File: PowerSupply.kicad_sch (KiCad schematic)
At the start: 31 parts, among them J1 B2B-PH-K-S, J2 Native USB, J3 Native USB, SW1 SSSS213000, U1 CH340E, U2 NCP1117-5.0_SOT223, U3 TPS2115ADRBR, U4 ld39150dt33-r, U5 USBLC6-2SC6, U6 USBLC6-2SC6

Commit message: update for production
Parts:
- renumbered Serial to Serial1
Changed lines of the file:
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@@
 		(on_board yes)
 		(dnp no)
-		(property "Reference" "#PWR0103"
+		(property "Reference" "#PWR024"
 			(at 107.95 179.07 0)
 			(effects
@@
 			(project "MX_IMU"
 				(path "/8ed38441-7d4e-4e89-870f-07e11c6dce38/623e427f-6907-46a8-ba12-bccc1b1d2c2b"
-					(reference "#PWR0103")
+					(reference "#PWR024")
 					(unit 1)
 				)
@@
 		(dnp no)
 		(fields_autoplaced yes)
-		(property "Reference" "#PWR030"
+		(property "Reference" "#PWR033"
 			(at 209.55 52.07 0)
 			(effects
@@
 			(project "MX_IMU"
 				(path "/8ed38441-7d4e-4e89-870f-07e11c6dce38/623e427f-6907-46a8-ba12-bccc1b1d2c2b"
-					(reference "#PWR030")
+					(reference "#PWR033")
 					(unit 1)
 				)
@@
 		(on_board yes)
 		(dnp no)
-		(property "Reference" "#PWR029"
+		(property "Reference" "#PWR032"
 			(at 166.37 143.51 0)
 			(effects
@@
 			(project "MX_IMU"
 				(path "/8ed38441-7d4e-4e89-870f-07e11c6dce38/623e427f-6907-46a8-ba12-bccc1b1d2c2b"
-					(reference "#PWR029")
+					(reference "#PWR032")
 					(unit 1)
 				)
@@
 		(dnp no)
 		(fields_autoplaced yes)
-		(property "Reference" "#PWR031"
+		(property "Reference" "#PWR034"
 			(at 209.55 114.3 0)
 			(effects
@@
 			(project "MX_IMU"
 				(path "/8ed38441-7d4e-4e89-870f-07e11c6dce38/623e427f-6907-46a8-ba12-bccc1b1d2c2b"
-					(reference "#PWR031")
+					(reference "#PWR034")
 					(unit 1)
 				)
@@
 		(dnp no)
 		(fields_autoplaced yes)
-		(property "Reference" "#PWR027"
+		(property "Reference" "#PWR030"
 			(at 138.43 111.76 0)
 			(effects
@@
 			(project "MX_IMU"
 				(path "/8ed38441-7d4e-4e89-870f-07e11c6dce38/623e427f-6907-46a8-ba12-bccc1b1d2c2b"
-					(reference "#PWR027")
+					(reference "#PWR030")
 					(unit 1)
 				)
@@
 		(on_board yes)
 		(dnp no)
-		(property "Reference" "#PWR024"
+		(property "Reference" "#PWR027"
 			(at 128.27 50.8 0)
 			(effects
@@
 			(project "MX_IMU"
 				(path "/8ed38441-7d4e-4e89-870f-07e11c6dce38/623e427f-6907-46a8-ba12-bccc1b1d2c2b"
-					(reference "#PWR024")
+					(reference "#PWR027")
 					(unit 1)
 				)
@@
 		(dnp no)
 		(fields_autoplaced yes)
-		(property "Reference" "#PWR032"
+		(property "Reference" "#PWR035"
 			(at 214.63 52.07 0)
 			(effects
@@
 			(project "MX_IMU"
 				(path "/8ed38441-7d4e-4e89-870f-07e11c6dce38/623e427f-6907-46a8-ba12-bccc1b1d2c2b"
-					(reference "#PWR032")
+					(reference "#PWR035")
 					(unit 1)
 				)
@@
 		(dnp no)
 		(fields_autoplaced yes)
-		(property "Reference" "#PWR034"
+		(property "Reference" "#PWR037"
 			(at 231.14 77.47 0)
 			(effects
@@
 			(project "MX_IMU"
 				(path "/8ed38441-7d4e-4e89-870f-07e11c6dce38/623e427f-6907-46a8-ba12-bccc1b1d2c2b"
-					(reference "#PWR034")
+					(reference "#PWR037")
 					(unit 1)
 				)
@@
 		(on_board yes)
 		(dnp no)
-		(property "Reference" "#PWR022"
+		(property "Reference" "#PWR025"
 			(at 102.87 50.8 0)
 			(effects
@@
 			(project "MX_IMU"
 				(path "/8ed38441-7d4e-4e89-870f-07e11c6dce38/623e427f-6907-46a8-ba12-bccc1b1d2c2b"
-					(reference "#PWR022")
+					(reference "#PWR025")
 					(unit 1)
 				)
@@
 		(dnp no)
 		(fields_autoplaced yes)
-		(property "Reference" "#PWR036"
+		(property "Reference" "#PWR039"
 			(at 251.46 130.81 0)
 			(effects
@@
 			(project "MX_IMU"
 				(path "/8ed38441-7d4e-4e89-870f-07e11c6dce38/623e427f-6907-46a8-ba12-bccc1b1d2c2b"
-					(reference "#PWR036")
+					(reference "#PWR039")
 					(unit 1)
 				)
@@
 		(on_board yes)
 		(dnp no)
-		(property "Reference" "Serial"
+		(property "Reference" "Serial1"
 			(at 89.154 171.45 0)
 			(effects
@@
 			(project "MX_IMU"
 				(path "/8ed38441-7d4e-4e89-870f-07e11c6dce38/623e427f-6907-46a8-ba12-bccc1b1d2c2b"
-					(reference "Serial")
+					(reference "Serial1")
 					(unit 1)
 				)
@@
 		(dnp no)
 		(fields_autoplaced yes)
-		(property "Reference" "#PWR023"
+		(property "Reference" "#PWR026"
 			(at 115.57 76.2 0)
 			(effects
@@
 			(project "MX_IMU"
 				(path "/8ed38441-7d4e-4e89-870f-07e11c6dce38/623e427f-6907-46a8-ba12-bccc1b1d2c2b"
-					(reference "#PWR023")
+					(reference "#PWR026")
 					(unit 1)
 				)
@@
 		(dnp no)
 		(fields_autoplaced yes)
-		(property "Reference" "#PWR033"
+		(property "Reference" "#PWR036"
 			(at 214.63 114.3 0)
 			(effects
@@
 			(project "MX_IMU"
 				(path "/8ed38441-7d4e-4e89-870f-07e11c6dce38/623e427f-6907-46a8-ba12-bccc1b1d2c2b"
-					(reference "#PWR033")
+					(reference "#PWR036")
 					(unit 1)
 				)
@@
 		(on_board yes)
 		(dnp no)
-		(property "Reference" "#PWR0102"
+		(property "Reference" "#PWR022"
 			(at 83.82 190.5 0)
 			(effects
@@
 			(project "MX_IMU"
 				(path "/8ed38441-7d4e-4e89-870f-07e11c6dce38/623e427f-6907-46a8-ba12-bccc1b1d2c2b"
-					(reference "#PWR0102")
+					(reference "#PWR022")
 					(unit 1)
 				)
@@
 		(on_board yes)
 		(dnp no)
-		(property "Reference" "#PWR0101"
+		(property "Reference" "#PWR021"
 			(at 83.82 180.34 0)
 			(effects
@@
 			(project "MX_IMU"
 				(path "/8ed38441-7d4e-4e89-870f-07e11c6dce38/623e427f-6907-46a8-ba12-bccc1b1d2c2b"
-					(reference "#PWR0101")
+					(reference "#PWR021")
 					(unit 1)
 				)
@@
 		(dnp no)
 		(fields_autoplaced yes)
-		(property "Reference" "#PWR025"
+		(property "Reference" "#PWR028"
 			(at 130.81 111.76 0)
 			(effects
@@
 			(project "MX_IMU"
 				(path "/8ed38441-7d4e-4e89-870f-07e11c6dce38/623e427f-6907-46a8-ba12-bccc1b1d2c2b"
-					(reference "#PWR025")
+					(reference "#PWR028")
 					(unit 1)
 				)
@@
 		(dnp no)
 		(fields_autoplaced yes)
-		(property "Reference" "#PWR035"
+		(property "Reference" "#PWR038"
 			(at 251.46 66.04 0)
 			(effects
@@
 			(project "MX_IMU"
 				(path "/8ed38441-7d4e-4e89-870f-07e11c6dce38/623e427f-6907-46a8-ba12-bccc1b1d2c2b"
-					(reference "#PWR035")
+					(reference "#PWR038")
 					(unit 1)
 				)
@@
 		(dnp no)
 		(fields_autoplaced yes)
-		(property "Reference" "#PWR026"
+		(property "Reference" "#PWR029"
 			(at 138.43 91.44 0)
 			(effects
@@
 			(project "MX_IMU"
 				(path "/8ed38441-7d4e-4e89-870f-07e11c6dce38/623e427f-6907-46a8-ba12-bccc1b1d2c2b"
-					(reference "#PWR026")
+					(reference "#PWR029")
 					(unit 1)
 				)
@@
 		(on_board yes)
 		(dnp no)
-		(property "Reference" "#PWR028"
+		(property "Reference" "#PWR031"
 			(at 166.37 81.28 0)
 			(effects
@@
 			(project "MX_IMU"
 				(path "/8ed38441-7d4e-4e89-870f-07e11c6dce38/623e427f-6907-46a8-ba12-bccc1b1d2c2b"
-					(reference "#PWR028")
+					(reference "#PWR031")
 					(unit 1)
 				)
@@
 		(dnp no)
 		(fields_autoplaced yes)
-		(property "Reference" "#PWR021"
+		(property "Reference" "#PWR023"
 			(at 86.36 121.92 0)
 			(effects
@@
 			(project "MX_IMU"
 				(path "/8ed38441-7d4e-4e89-870f-07e11c6dce38/623e427f-6907-46a8-ba12-bccc1b1d2c2b"
-					(reference "#PWR021")
+					(reference "#PWR023")
 					(unit 1)
 				)

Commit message: PumbaaV2_RC2
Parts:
- C7: JLCPCB part (none) -> C15849
- R2, R3: value 330 -> 330R
- Serial1: value SM04B-GHS-TB -> SM04B-GHS-TB(LF)(SN)
- U2: value NCP1117-5.0_SOT223 -> NCP1117ST50T3G; JLCPCB Part (none) -> C17314
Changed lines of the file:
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@@
 			)
 		)
-		(property "Value" "NCP1117-5.0_SOT223"
+		(property "Value" "NCP1117ST50T3G"
 			(at 69.85 51.5421 0)
 			(effects
@@
 					(size 1.27 1.27)
 				)
+			)
+		)
+		(property "JLCPCB Part" "C17314"
+			(at 69.85 54.61 0)
+			(effects
+				(font
+					(size 1.27 1.27)
+				)
+				(hide yes)
 			)
 		)
@@
 			)
 		)
+		(property "JLCPCB part" "C15849"
+			(at 102.87 59.69 0)
+			(effects
+				(font
+					(size 1.27 1.27)
+				)
+				(hide yes)
+			)
+		)
 		(pin "1"
 		)
@@
 			)
 		)
-		(property "Value" "330"
+		(property "Value" "330R"
 			(at 71.12 149.86 0)
 			(effects
@@
 			)
 		)
-		(property "Value" "330"
+		(property "Value" "330R"
 			(at 62.23 149.86 0)
 			(effects
@@
 			)
 		)
-		(property "Value" "SM04B-GHS-TB"
+		(property "Value" "SM04B-GHS-TB(LF)(SN)"
 			(at 97.79 181.6099 0)
 			(effects

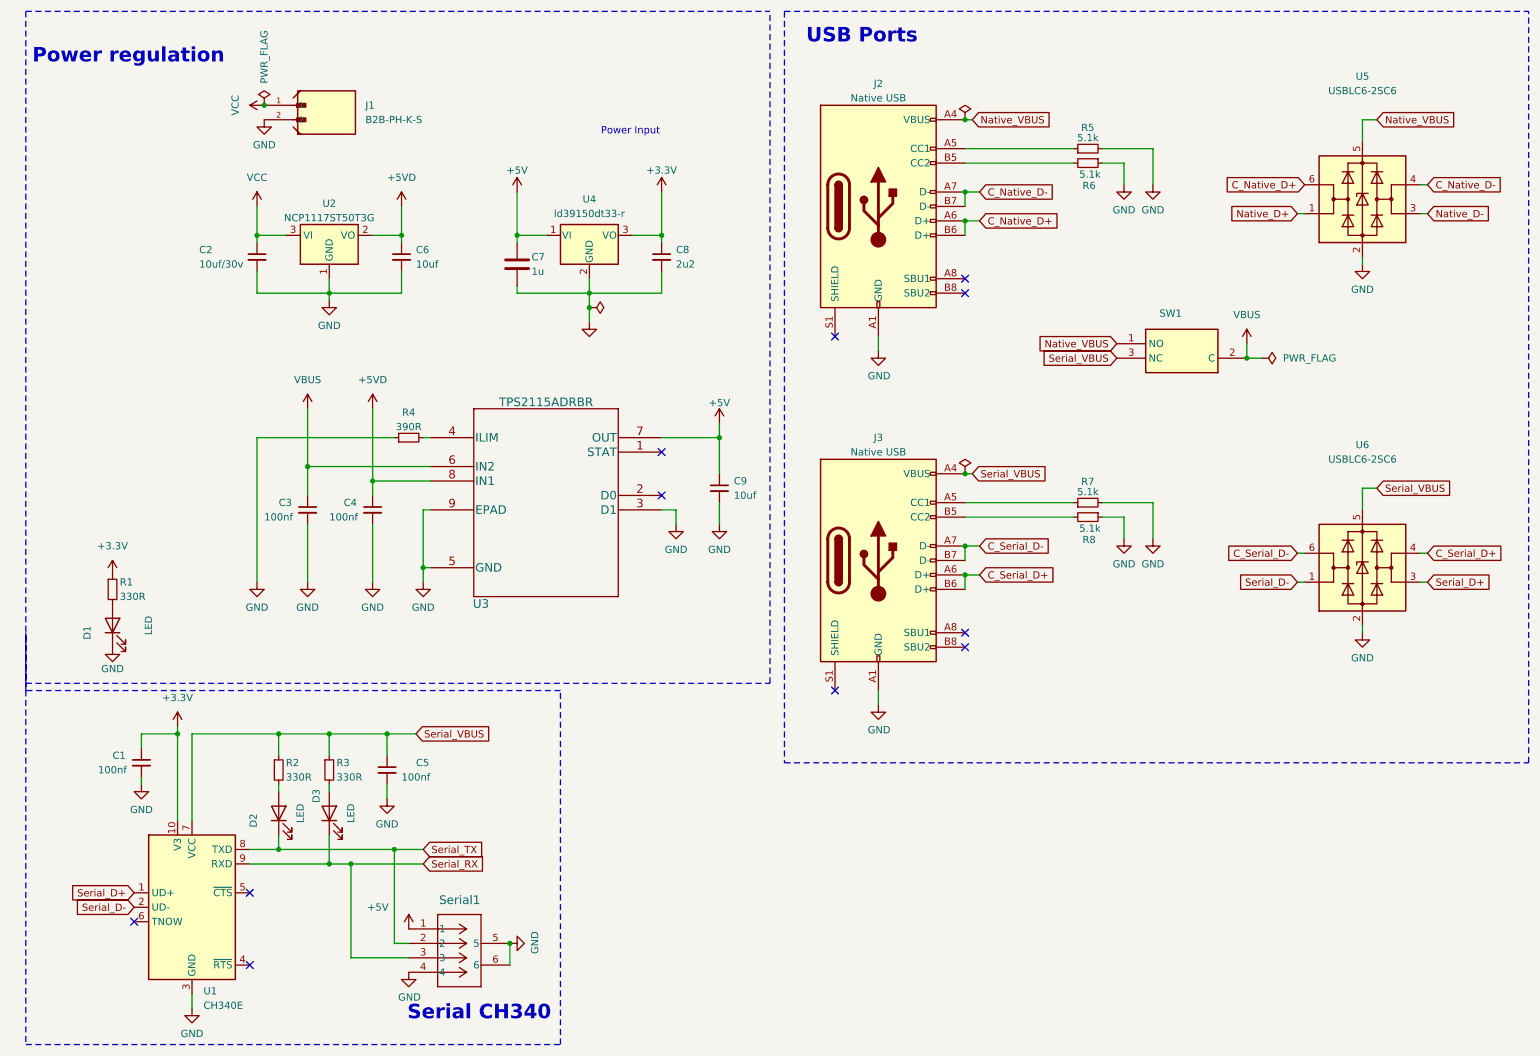
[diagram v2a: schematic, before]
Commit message: compact  IMU module for integration
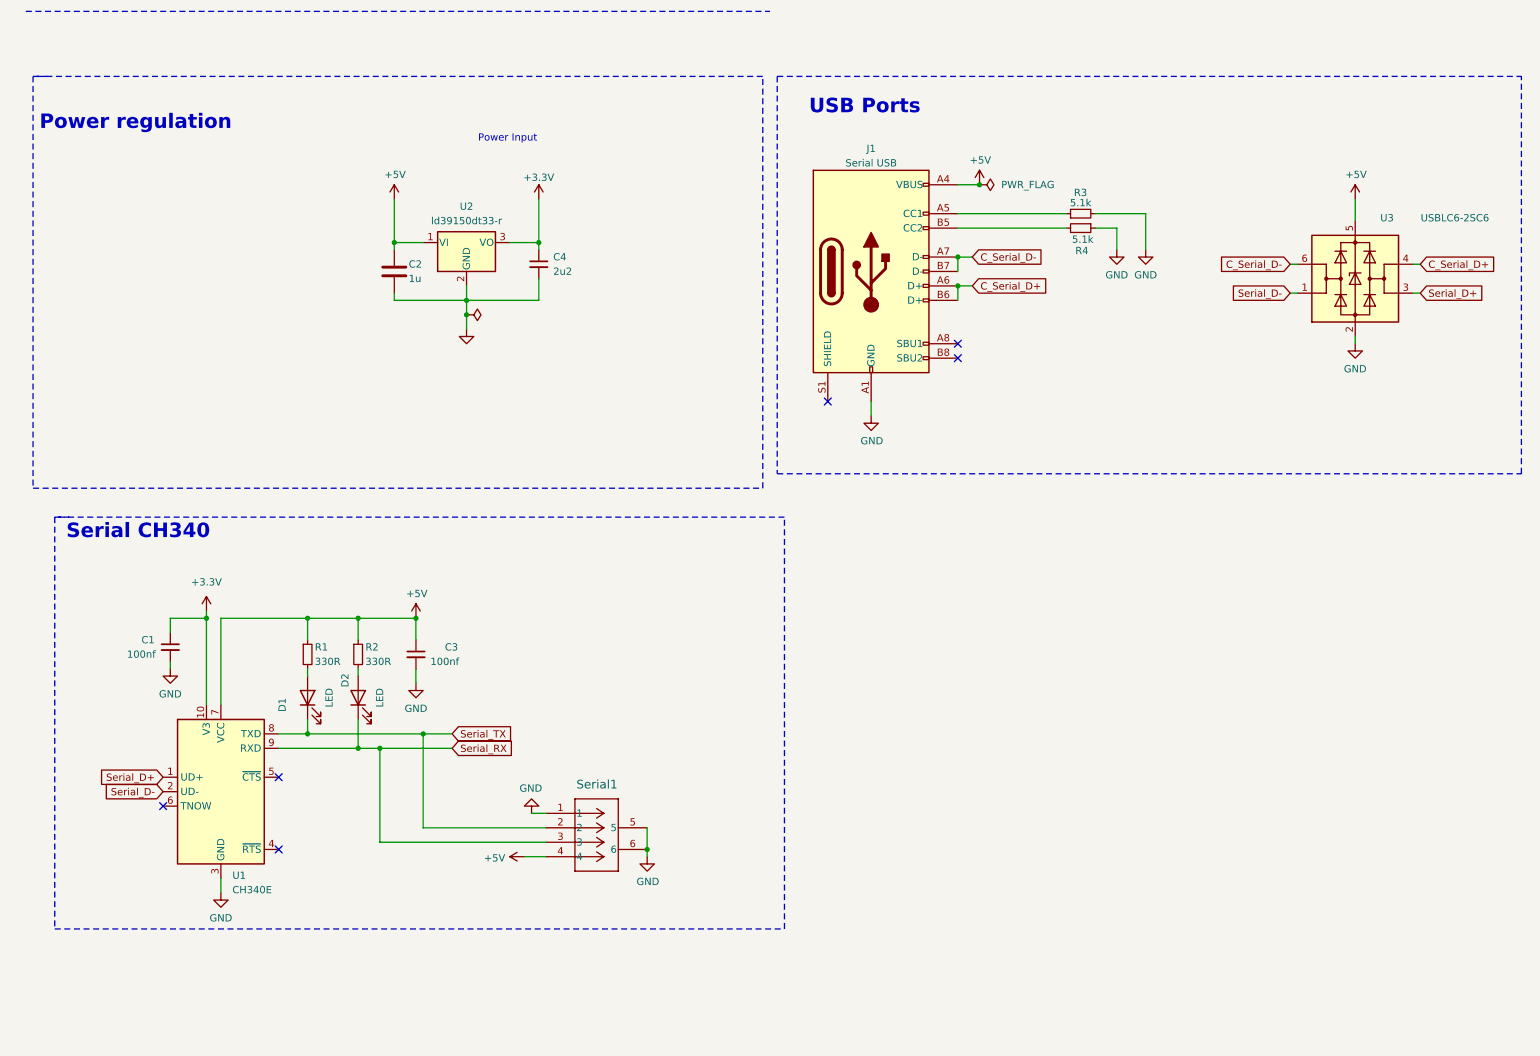
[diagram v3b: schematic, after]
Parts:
- removed C2: 10uf/30v, Capacitor_SMD:C_0805_2012Metric, symbol Device:C_Small
- removed C3, C4: 100nf, Capacitor_SMD:C_0603_1608Metric, symbol Device:C_Small
- removed C6, C9: 10uf, Capacitor_SMD:C_0603_1608Metric, symbol Device:C_Small
- removed D1: LED, LED_SMD:LED_0603_1608Metric, symbol Device:LED
- removed J1: B2B-PH-K-S, mylib:JST_B2B-PH-K-S, symbol B2B-PH-K-S:B2B-PH-K-S
- removed J2: Native USB, Connector_USB:USB_C_Receptacle_HRO_TYPE-C-31-M-12, symbol usb_c_receptacle_usb2.0:USB_C_Receptacle_USB2.0
- removed R1: 330R, Resistor_SMD:R_0402_1005Metric, symbol Device:R_Small
- removed R4: 390R, Resistor_SMD:R_0603_1608Metric, symbol Device:R_Small
- removed R5, R6: 5.1k, Resistor_SMD:R_0603_1608Metric, symbol Device:R_Small
- removed SW1: SSSS213000, mylib:SSSS213000, symbol SSSS213000:SSSS213000
- removed U2: NCP1117ST50T3G, Package_TO_SOT_SMD:SOT-223-3_TabPin2, symbol Regulator_Linear:NCP1117-5.0_SOT223
- removed U3: TPS2115ADRBR, mylib:SON65P300X300X100-9N, symbol tps2115adrbr:TPS2115ADRBR
- removed U5: USBLC6-2SC6, Package_TO_SOT_SMD:SOT-23-6, symbol usblc6-2sc6:USBLC6-2SC6
- J1: renamed from J3; value Native USB -> Serial USB
- renumbered C7 to C2, C5 to C3, C8 to C4, D2 to D1, D3 to D2, R2 to R1, R3 to R2, R7 to R3, R8 to R4, U4 to U2, U6 to U3
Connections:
- net Serial_VBUS is gone; now on net +5V: C3.1, J1.A4 (VBUS), J1.A9 (VBUS), J1.B4 (VBUS), J1.B9 (VBUS), R1.1, R2.1, U1.7 (VCC), U3.5 (VBUS)
- net +5V: now also Serial1.4; no longer Serial1.1
- net GND: now also Serial1.1; no longer Serial1.4
- no-connect marks 11 -> 6
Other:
- moved on the sheet: C1, C2, C3, C4, D1, D2, J1, R1, R2, R3, R4, Serial1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

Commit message: IMU_IMU V1.0 is ready.
correct ch340e
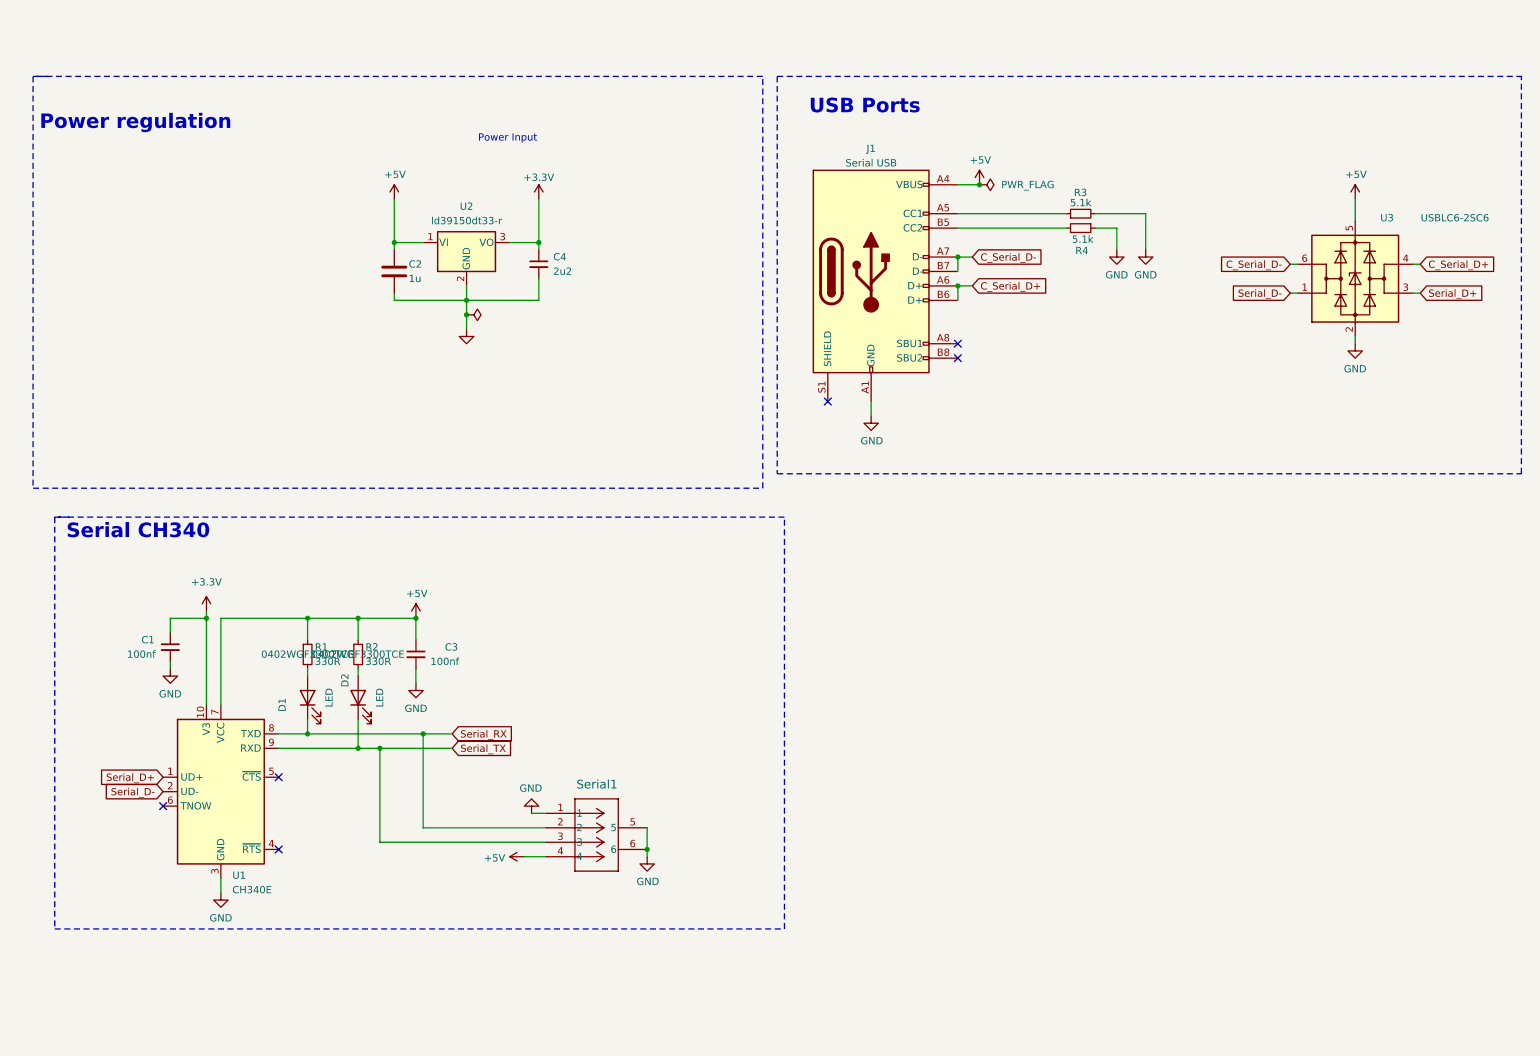
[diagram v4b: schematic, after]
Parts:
- R1, R2: LCSC Part # C25744 -> C25104
- U1: footprint Package_SO:MSOP-10_3x3mm_P0.5mm -> mylib:MSOP-10_3x3mm_P0.5mm
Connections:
- net Serial_RX: now also D1.1 (K), Serial1.2, U1.8 (TXD); no longer D2.1 (K), Serial1.3, U1.9 (RXD)
- net Serial_TX: now also D2.1 (K), Serial1.3, U1.9 (RXD); no longer D1.1 (K), Serial1.2, U1.8 (TXD)
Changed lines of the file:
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@@
-		)
-	)
-	(polyline
-		(pts
-			(xy 16.51 15.24) (xy 147.32 15.24)
-		)
-		(stroke
-			(width 0)
-			(type dash)
 		)
 	)
@@
 		)
 	)
-	(global_label "Serial_TX"
-		(shape input)
-		(at 91.44 142.24 0)
-		(effects
-			(font
-				(size 1.27 1.27)
-			)
-			(justify left)
-		)
-		(property "Intersheetrefs" "${INTERSHEET_REFS}"
-			(at 91.44 142.24 0)
-			(effects
-				(font
-					(size 1.27 1.27)
-				)
-				(hide yes)
-			)
-		)
-	)
 	(global_label "Serial_D+"
 		(shape input)
@@
 		)
 	)
-	(global_label "Serial_RX"
-		(shape input)
-		(at 91.44 144.78 0)
-		(effects
-			(font
-				(size 1.27 1.27)
-			)
-			(justify left)
-		)
-		(property "Intersheetrefs" "${INTERSHEET_REFS}"
-			(at 91.44 144.78 0)
-			(effects
-				(font
-					(size 1.27 1.27)
-				)
-				(hide yes)
-			)
-		)
-	)
 	(global_label "C_Serial_D+"
 		(shape input)
@@
 		)
 	)
+	(global_label "Serial_TX"
+		(shape input)
+		(at 91.44 144.78 0)
+		(effects
+			(font
+				(size 1.27 1.27)
+			)
+			(justify left)
+		)
+		(property "Intersheetrefs" "${INTERSHEET_REFS}"
+			(at 91.44 144.78 0)
+			(effects
+				(font
+					(size 1.27 1.27)
+				)
+				(hide yes)
+			)
+		)
+	)
 	(global_label "C_Serial_D-"
 		(shape input)
@@
 				)
 				(justify left)
+				(hide yes)
+			)
+		)
+	)
+	(global_label "Serial_RX"
+		(shape input)
+		(at 91.44 142.24 0)
+		(effects
+			(font
+				(size 1.27 1.27)
+			)
+			(justify left)
+		)
+		(property "Intersheetrefs" "${INTERSHEET_REFS}"
+			(at 91.44 142.24 0)
+			(effects
+				(font
+					(size 1.27 1.27)
+				)
 				(hide yes)
 			)
@@
 			)
 		)
-		(property "Footprint" "Package_SO:MSOP-10_3x3mm_P0.5mm"
+		(property "Footprint" "mylib:MSOP-10_3x3mm_P0.5mm"
 			(at 52.07 166.37 0)
 			(effects
@@
 			)
 		)
-		(property "Description" ""
+		(property "Description" "0402WGF3300TCE"
 			(at 74.93 128.27 0)
 			(effects
@@
 			)
 		)
-		(property "LCSC Part #" "C25744"
+		(property "LCSC Part #" "C25104"
 			(at 74.93 128.27 0)
 			(effects
@@
 			)
 		)
-		(property "Description" ""
+		(property "Description" "0402WGF3300TCE"
 			(at 66.04 128.27 0)
 			(effects
@@
 			)
 		)
-		(property "LCSC Part #" "C25744"
+		(property "LCSC Part #" "C25104"
 			(at 66.04 128.27 0)
 			(effects
